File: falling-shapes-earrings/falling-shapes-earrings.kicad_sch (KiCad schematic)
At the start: 0 parts

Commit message: Update falling-shapes-earrings.kicad_sch
Added symbols to schematic
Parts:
- added C1: 100nF, symbol Capacitors:GCD21BR72A104KA01L
- added D1: (no value), symbol Optoelectronics:WS2812B-2020
- added U1: (no value), symbol IC - Microcontrollers:ATTiny85
- added XBT1: (no value), symbol Power:SMTU1632-LF
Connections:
- new net: C1.2, U1.8 (VCC)

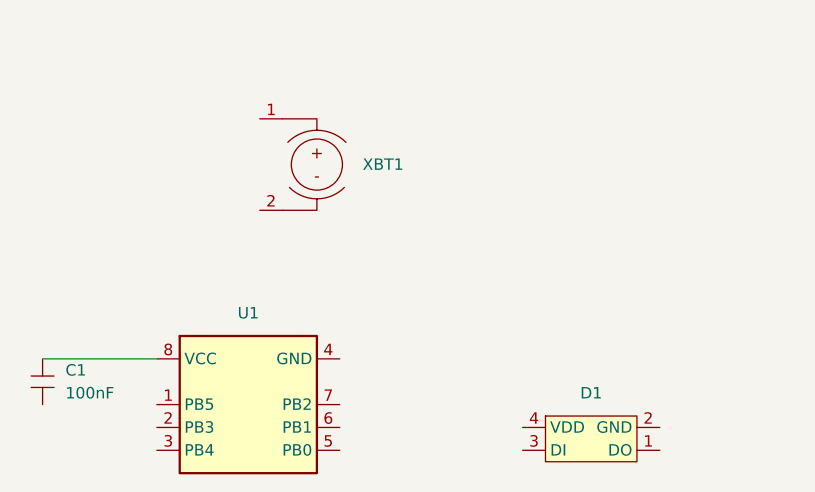
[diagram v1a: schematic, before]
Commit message: Update falling-shapes-earrings.kicad_sch
Adding power symbols
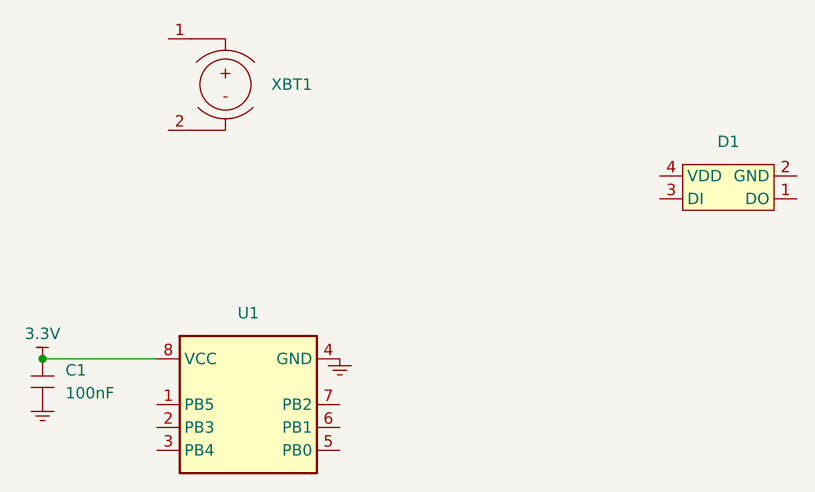
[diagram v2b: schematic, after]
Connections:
- net 3.3V: now reaches C1.2, U1.8 (VCC)
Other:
- moved on the sheet: D1, XBT1

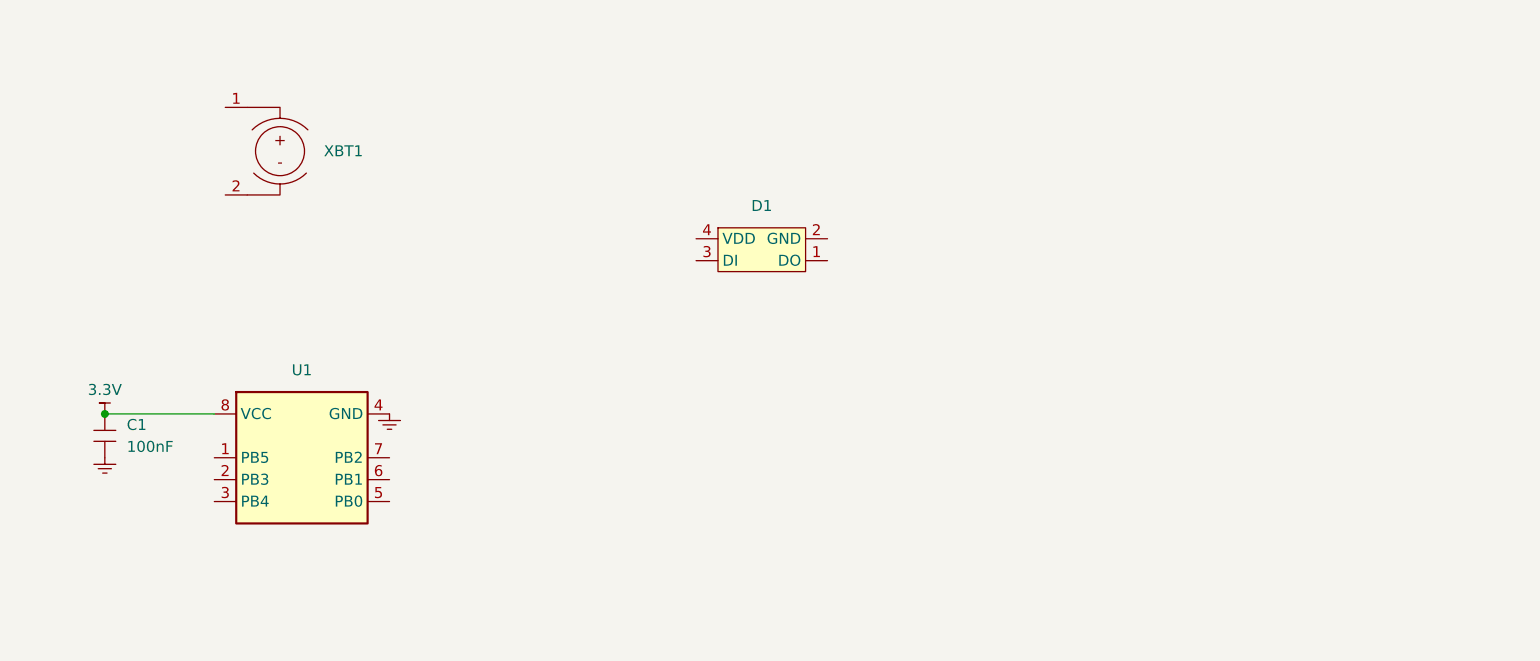
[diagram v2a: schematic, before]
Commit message: Update falling-shapes-earrings.kicad_sch
Annotation changes and capacitor changes
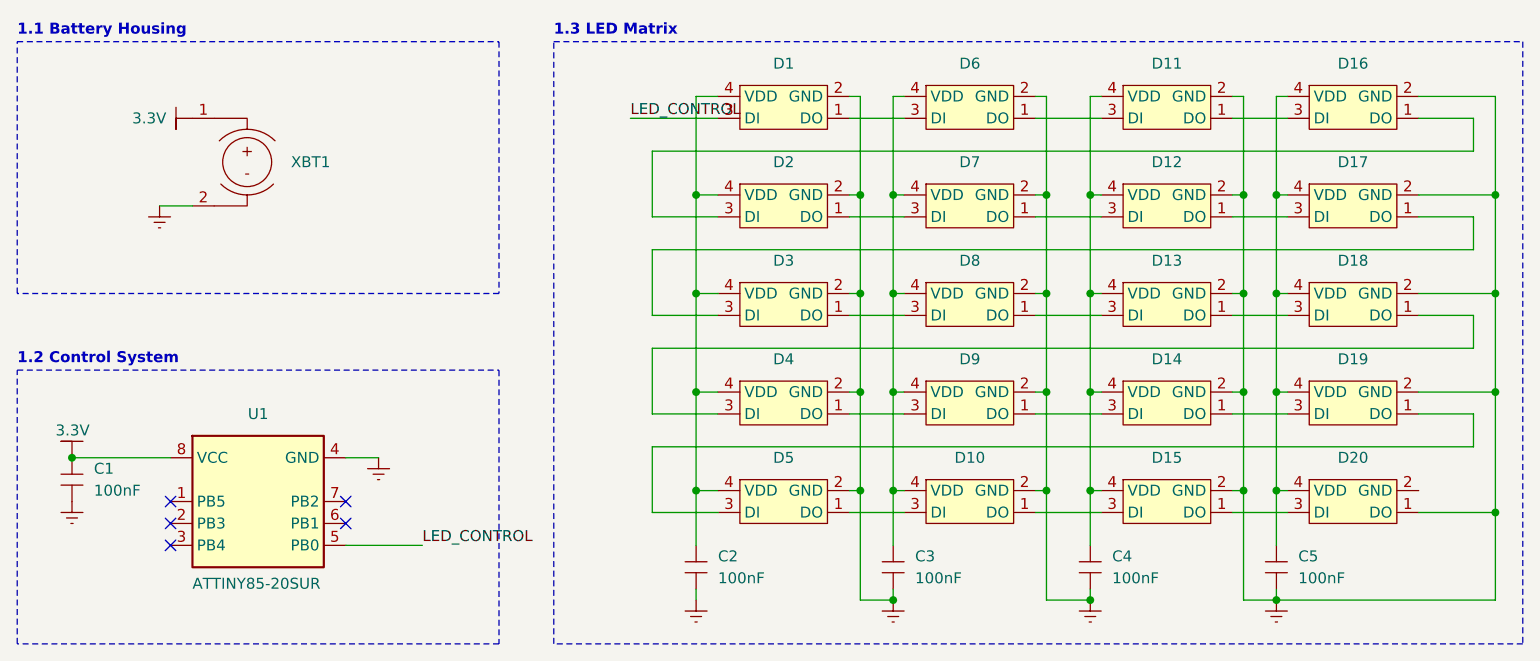
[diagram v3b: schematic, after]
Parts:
- added C2, C3, C4, C5: 100nF, symbol Capacitors:GCD21BR72A104KA01L
- added D10, D11, D12, D13, D14, D15, D16, D17, D18, D19, D2, D20, D3, D4, D5, D6, D7, D8, D9: (no value), symbol Optoelectronics:WS2812B-2020
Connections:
- net 3.3V: now also XBT1.1
- net at D1.1 (DO): now also D6.3 (DI)
- net GNDREF: now reaches D1.2 (GND)
- net GNDREF: now also C1.1, U1.4 (GND), XBT1.2, C2.1, C3.1, C4.1, C5.1, D10.2 (GND), D11.2 (GND), D12.2 (GND), D13.2 (GND), D14.2 (GND), D15.2 (GND), D16.2 (GND), D17.2 (GND), D18.2 (GND), D19.2 (GND), D2.2 (GND), D20.1 (DO), D3.2 (GND), D4.2 (GND), D5.2 (GND), D6.2 (GND), D7.2 (GND), D8.2 (GND), D9.2 (GND)
- net LED_CONTROL: now reaches D1.3 (DI)
- net LED_CONTROL: now also U1.5 (PB0)
- net at D1.4 (VDD): now also C2.2, D2.4 (VDD), D3.4 (VDD), D4.4 (VDD), D5.4 (VDD)
- new net: D19.1 (DO), D5.3 (DI)
- new net: D14.1 (DO), D19.3 (DI)
- new net: C5.2, D16.4 (VDD), D17.4 (VDD), D18.4 (VDD), D19.4 (VDD), D20.4 (VDD)
- new net: D14.3 (DI), D9.1 (DO)
- new net: C4.2, D11.4 (VDD), D12.4 (VDD), D13.4 (VDD), D14.4 (VDD), D15.4 (VDD)
- new net: D15.1 (DO), D20.3 (DI)
- new net: D10.1 (DO), D15.3 (DI)
- new net: D4.1 (DO), D9.3 (DI)
- new net: D18.1 (DO), D4.3 (DI)
- new net: D3.1 (DO), D8.3 (DI)
- new net: D17.1 (DO), D3.3 (DI)
- new net: D13.1 (DO), D18.3 (DI)
- new net: D13.3 (DI), D8.1 (DO)
- new net: D12.3 (DI), D7.1 (DO)
- new net: D2.1 (DO), D7.3 (DI)
- new net: C3.2, D10.4 (VDD), D6.4 (VDD), D7.4 (VDD), D8.4 (VDD), D9.4 (VDD)
- new net: D16.1 (DO), D2.3 (DI)
- new net: D11.1 (DO), D16.3 (DI)
- new net: D12.1 (DO), D17.3 (DI)
- new net: D10.3 (DI), D5.1 (DO)
- new net: D11.3 (DI), D6.1 (DO)
- no-connect marks 0 -> 5
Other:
- note added: "1.1 Battery Housing"
- note added: "1.2 Control System"
- note added: "1.3 LED Matrix"
- moved on the sheet: C1, D1, U1, XBT1
